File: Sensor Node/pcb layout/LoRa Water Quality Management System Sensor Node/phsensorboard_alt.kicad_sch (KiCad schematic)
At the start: 16 parts, among them U11 TL082, U12 LM2660MX

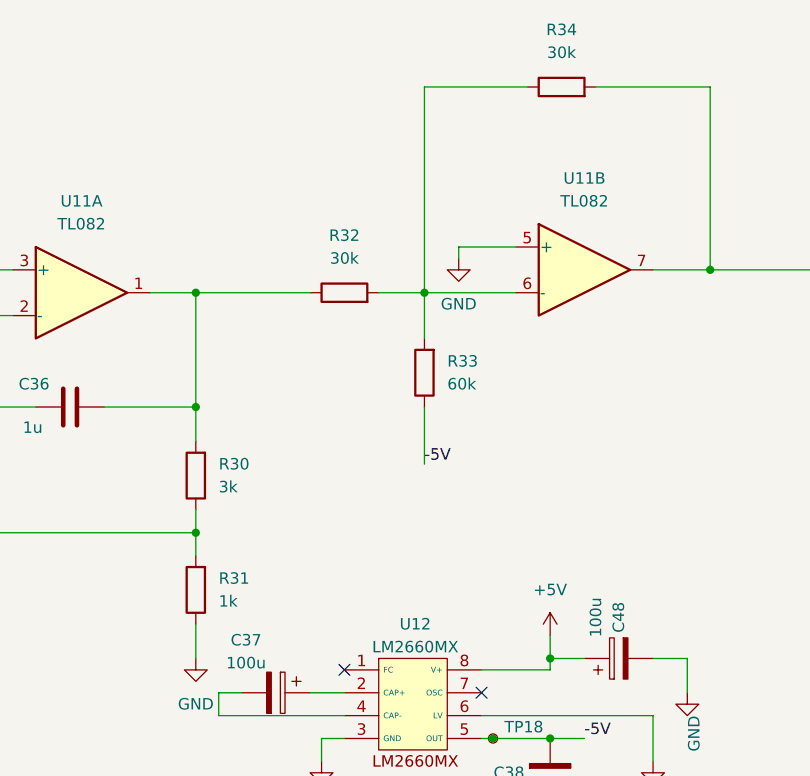
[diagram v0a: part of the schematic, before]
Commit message: Implemented RDT3.0 for LoRa data transfer.
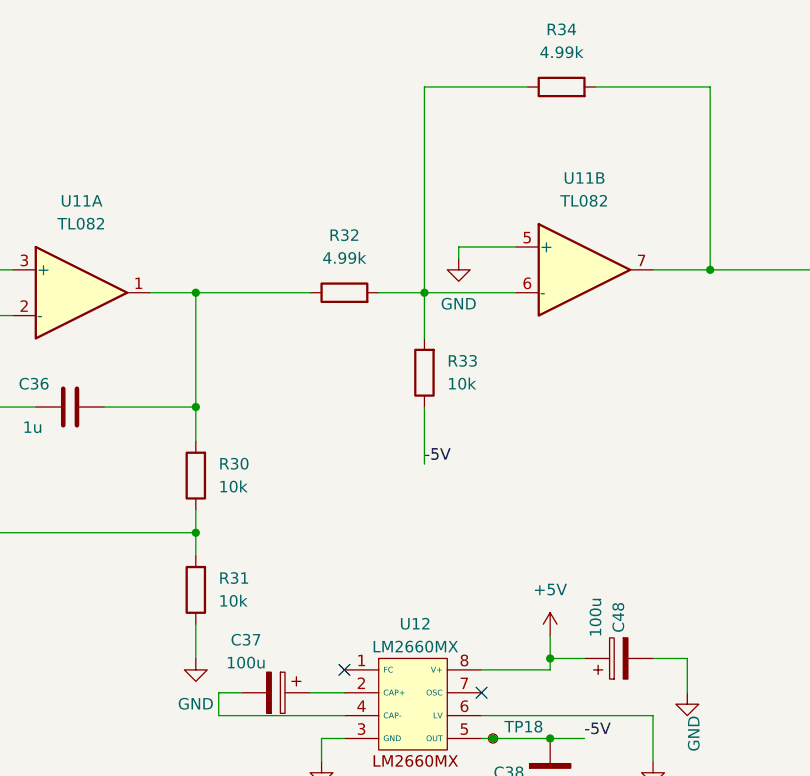
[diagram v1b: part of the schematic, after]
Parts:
- R30: value 3k -> 10k
- R31: value 1k -> 10k
- R32, R34: value 30k -> 4.99k
- R33: value 60k -> 10k
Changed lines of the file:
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@@
 			)
 		)
-		(property "Value" "3k"
+		(property "Value" "10k"
 			(at 151.13 97.7899 0)
 			(effects
@@
 			)
 		)
-		(property "Value" "30k"
+		(property "Value" "4.99k"
 			(at 165.1 72.39 90)
 			(effects
@@
 			)
 		)
-		(property "Value" "1k"
+		(property "Value" "10k"
 			(at 151.13 110.4899 0)
 			(effects
@@
 			)
 		)
-		(property "Value" "30k"
+		(property "Value" "4.99k"
 			(at 189.23 49.53 90)
 			(effects
@@
 			)
 		)
-		(property "Value" "60k"
+		(property "Value" "10k"
 			(at 176.53 86.3599 0)
 			(effects

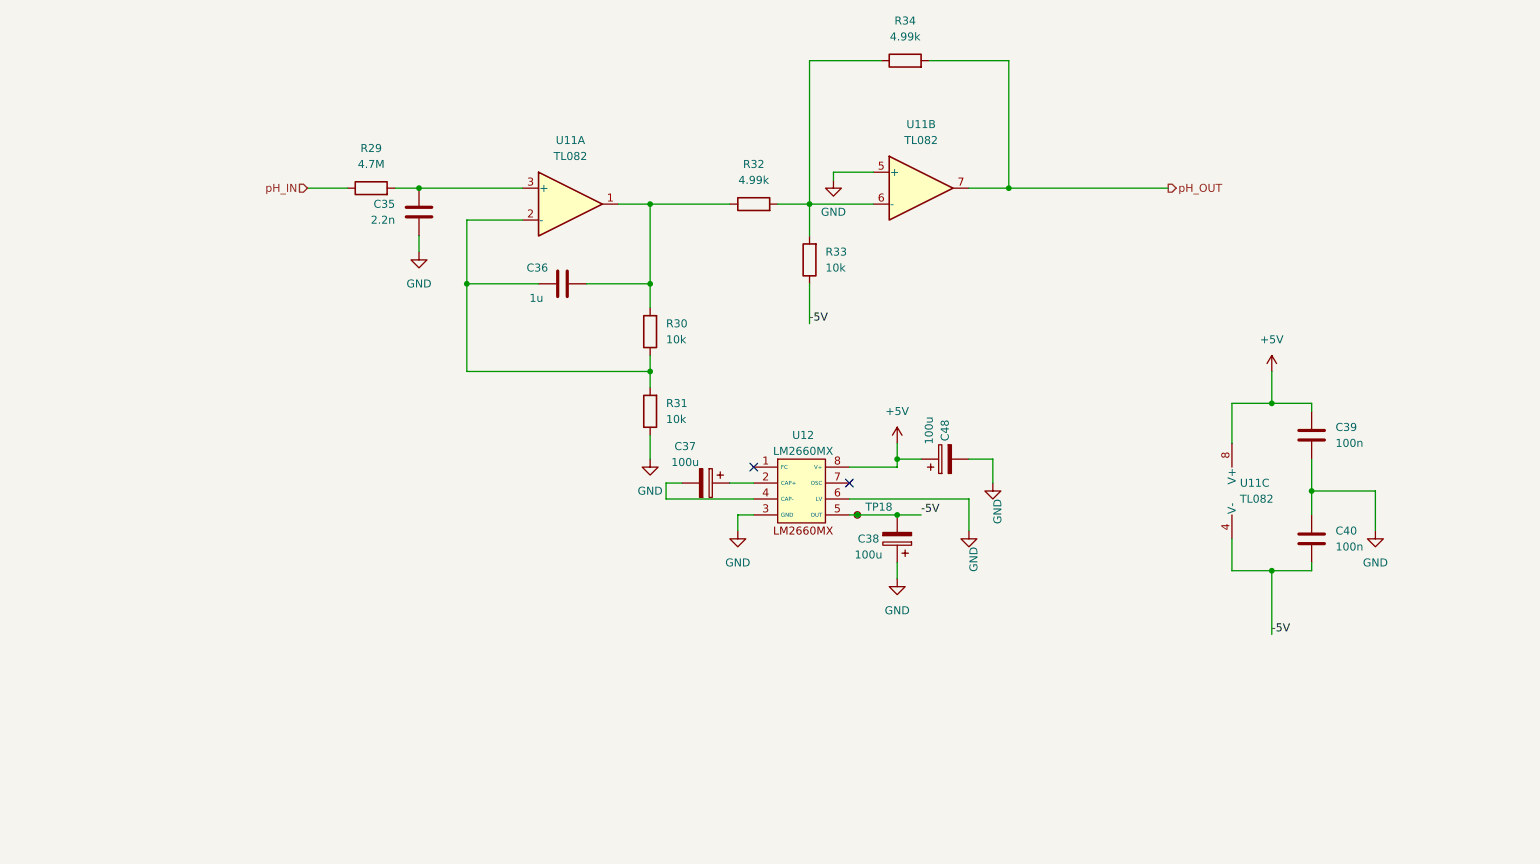
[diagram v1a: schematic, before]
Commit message: Finalize working software-defined instrumentation amplifier driver code and signal acquisition, begin prototyping sensor data conversion methods. Add hardware changes needed for expected operation of analog front-end.
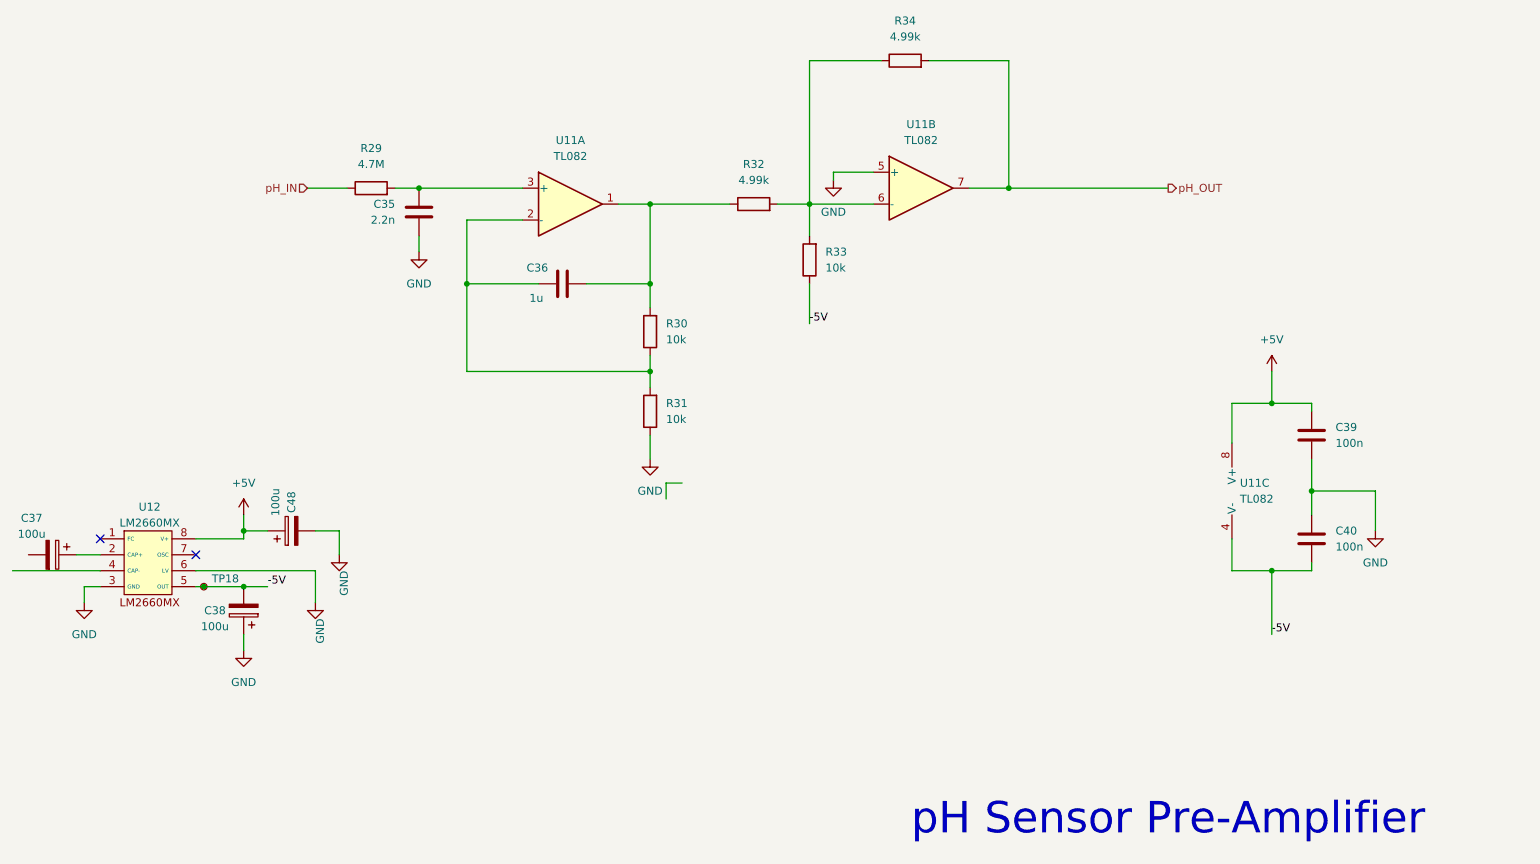
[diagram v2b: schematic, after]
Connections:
- net at C37.2: no longer U12.4 (CAP-)
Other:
- note added: "pH Sensor Pre-Amplifier"
- moved on the sheet: C37, C38, C48, TP18, U12

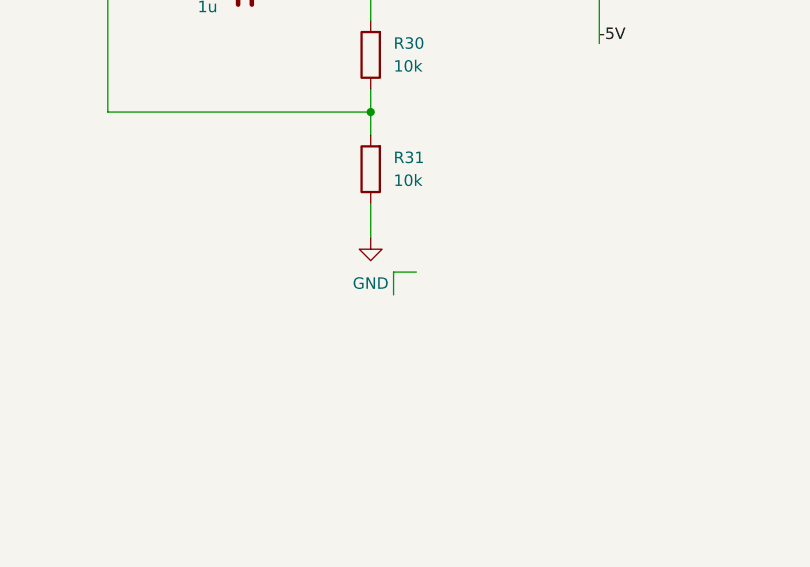
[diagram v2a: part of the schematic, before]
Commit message: Add finalized firmware - implemented power savings mode and implemented complete FSM.
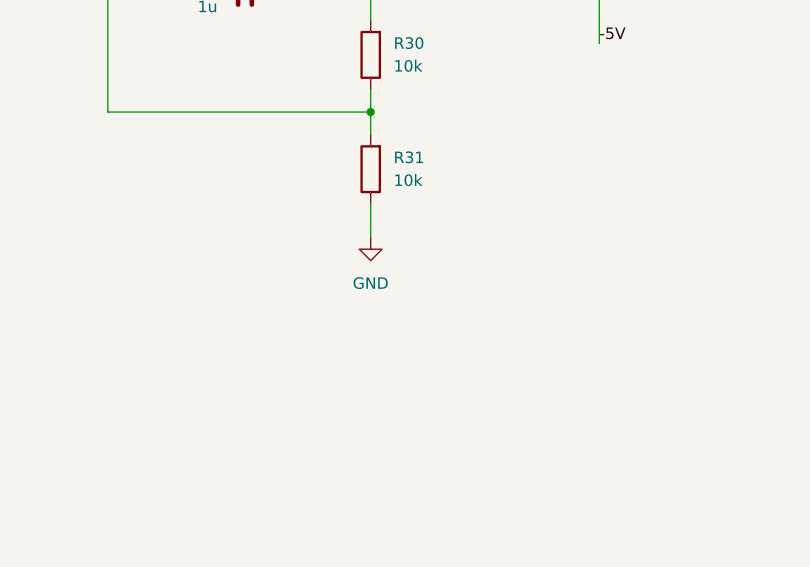
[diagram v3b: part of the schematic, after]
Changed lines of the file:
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@@
-	(wire
-		(pts
-			(xy 151.13 120.65) (xy 153.67 120.65)
-		)
-		(stroke
-			(width 0)
-			(type default)
-		)
-	)
 	(wire
 		(pts
@@
 		)
 		(stroke
-			(width 0)
-			(type default)
-		)
-	)
-	(wire
-		(pts
-			(xy 151.13 123.19) (xy 151.13 120.65)
-		)
-		(stroke
